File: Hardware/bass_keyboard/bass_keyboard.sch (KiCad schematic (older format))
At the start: 164 parts

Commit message: Added labels to switches
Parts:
- gave numbers to parts that had none: 82

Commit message: Added footprints for diodes
Having trouble finding the footprints for the switches
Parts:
- D1: renamed from D; footprint (none) -> Diode_SMD:D_SOD-123
- D10, D11, D12, D13, D14, D15, D16, D17, D18, D19, D2, D20, D21, D22, D23, D24, D25, D26, D27, D28, D29, D3, D30, D31, D32, D33, D34, D35, D36, D37, D38, D39, D4, D40, D41, D42, D43, D44, D45, D46, D47, D48, D49, D5, D50, D51, D52, D53, D54, D55, D56, D57, D58, D59, D6, D60, D61, D62, D63, D64, D65, D66, D67, D68, D69, D7, D70, D71, D72, D73, D74, D75, D76, D77, D78, D79, D8, D80, D81, D82, D9: renamed from D?; footprint (none) -> Diode_SMD:D_SOD-123
- renumbered MX_Ab-root to MX_Ab-root1, MX_Ab_3rd to MX_Ab_3rd1, MX_Ab_dim to MX_Ab_dim1, MX_Ab_maj to MX_Ab_maj1, MX_Ab_min to MX_Ab_min1, MX_An_3rd to MX_An_3rd1, MX_An_dim to MX_An_dim1, MX_An_maj to MX_An_maj1, MX_An_min to MX_An_min1, MX_An_root to MX_An_root1, MX_Bb_3rd to MX_Bb_3rd1, MX_Bb_dim to MX_Bb_dim1, MX_Bb_maj to MX_Bb_maj1, MX_Bb_min to MX_Bb_min1, MX_Bb_root to MX_Bb_root1, MX_Bn_3rd to MX_Bn_3rd1, MX_Bn_dim to MX_Bn_dim1, MX_Bn_maj to MX_Bn_maj1, MX_Bn_min to MX_Bn_min1, MX_Bn_root to MX_Bn_root1, MX_Cn_3rd to MX_Cn_3rd1, MX_Cn_dim to MX_Cn_dim1, MX_Cn_maj to MX_Cn_maj1, MX_Cn_min to MX_Cn_min1, MX_Cn_root to MX_Cn_root1, MX_Db_3rd to MX_Db_3rd1, MX_Db_dim to MX_Db_dim1, MX_Db_maj to MX_Db_maj1, MX_Db_min to MX_Db_min1, MX_Db_root to MX_Db_root1, MX_Dn_3rd to MX_Dn_3rd1, MX_Dn_dim to MX_Dn_dim1, MX_Dn_maj to MX_Dn_maj1, MX_Dn_min to MX_Dn_min1, MX_Dn_root to MX_Dn_root1, MX_Eb_3rd to MX_Eb_3rd1, MX_Eb_dim to MX_Eb_dim1, MX_Eb_maj to MX_Eb_maj1, MX_Eb_min to MX_Eb_min1, MX_Eb_root to MX_Eb_root1, MX_En_3rd to MX_En_3rd1, MX_En_dim to MX_En_dim1, MX_En_maj to MX_En_maj1, MX_En_min to MX_En_min1, MX_En_root to MX_En_root1, MX_Fn_3rd to MX_Fn_3rd1, MX_Fn_dim to MX_Fn_dim1, MX_Fn_maj to MX_Fn_maj1, MX_Fn_min to MX_Fn_min1, MX_Fn_root to MX_Fn_root1, MX_Fs_3rd to MX_Fs_3rd1, MX_Fs_dim to MX_Fs_dim1, MX_Fs_maj to MX_Fs_maj1, MX_Fs_min to MX_Fs_min1, MX_Fs_root to MX_Fs_root1, MX_Gn_3rd to MX_Gn_3rd1, MX_Gn_dim to MX_Gn_dim1, MX_Gn_maj to MX_Gn_maj1, MX_Gn_min to MX_Gn_min1, MX_Gn_root to MX_Gn_root1, MX_bassbar to MX_bassbar1, MX_dim_aug to MX_dim_aug1, MX_down_half to MX_down_half1, MX_down_oct to MX_down_oct1, MX_keysel_left to MX_keysel_left1, MX_keysel_right to MX_keysel_right1, MX_maj_dom to MX_maj_dom1, MX_trans_reset to MX_trans_reset1, MX_up_half to MX_up_half1, MX_up_oct to MX_up_oct1

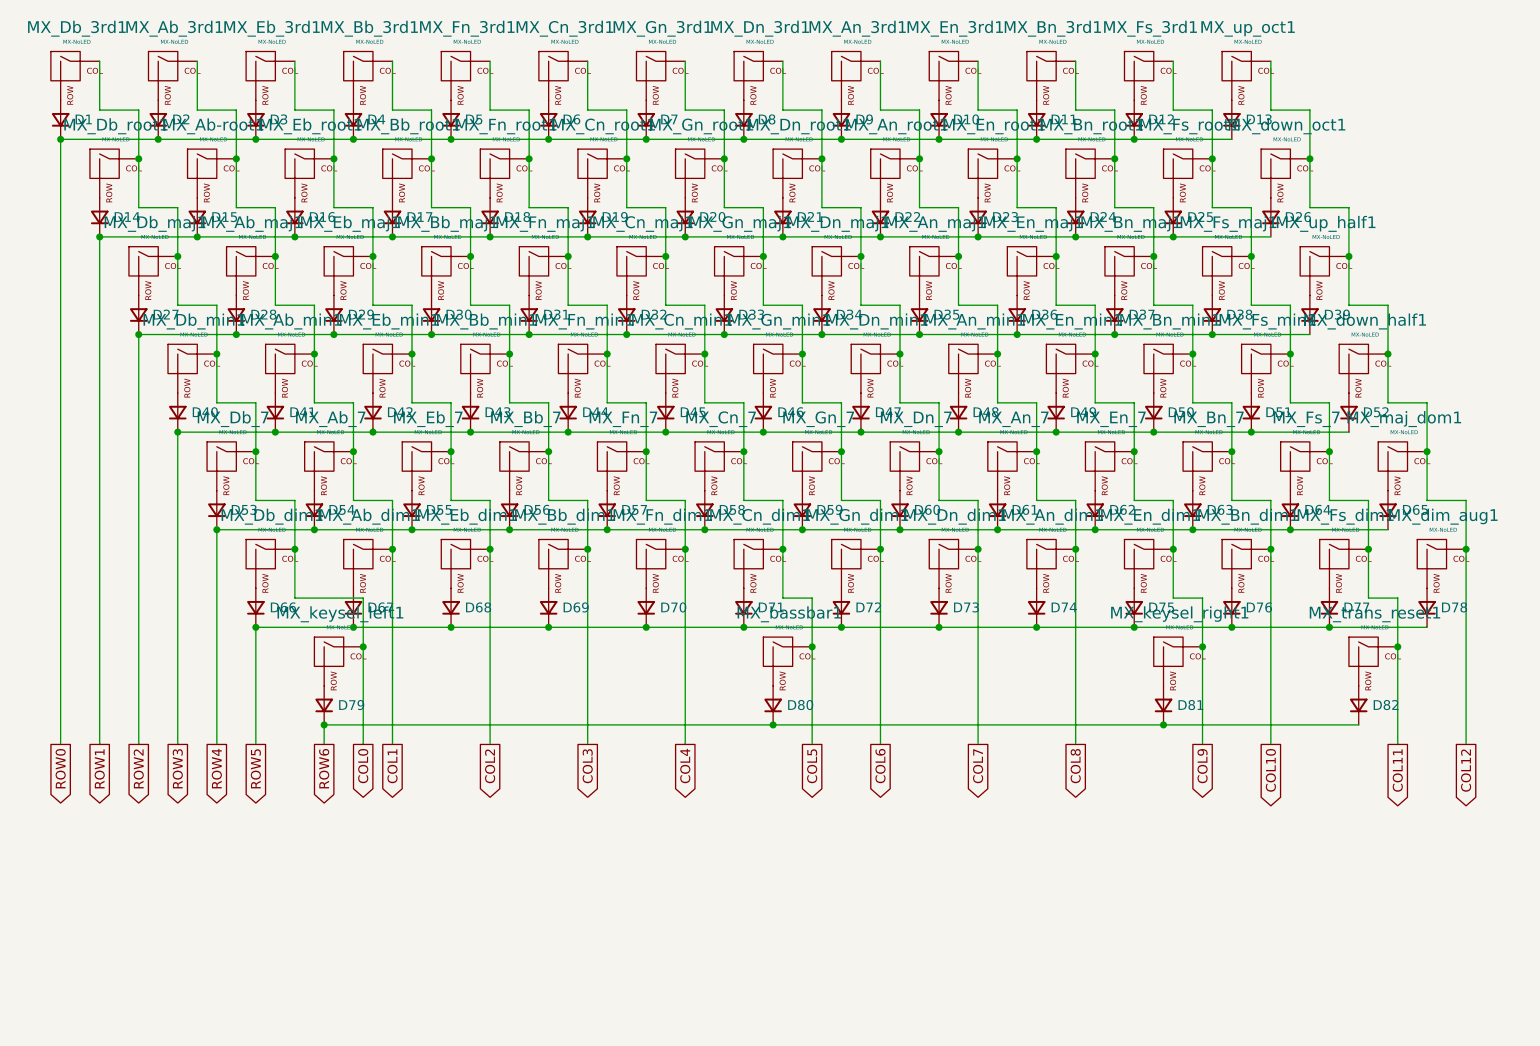
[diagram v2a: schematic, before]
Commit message: Added female connector
Added the connector for the cable to the logic module on the bass keyboard schematic
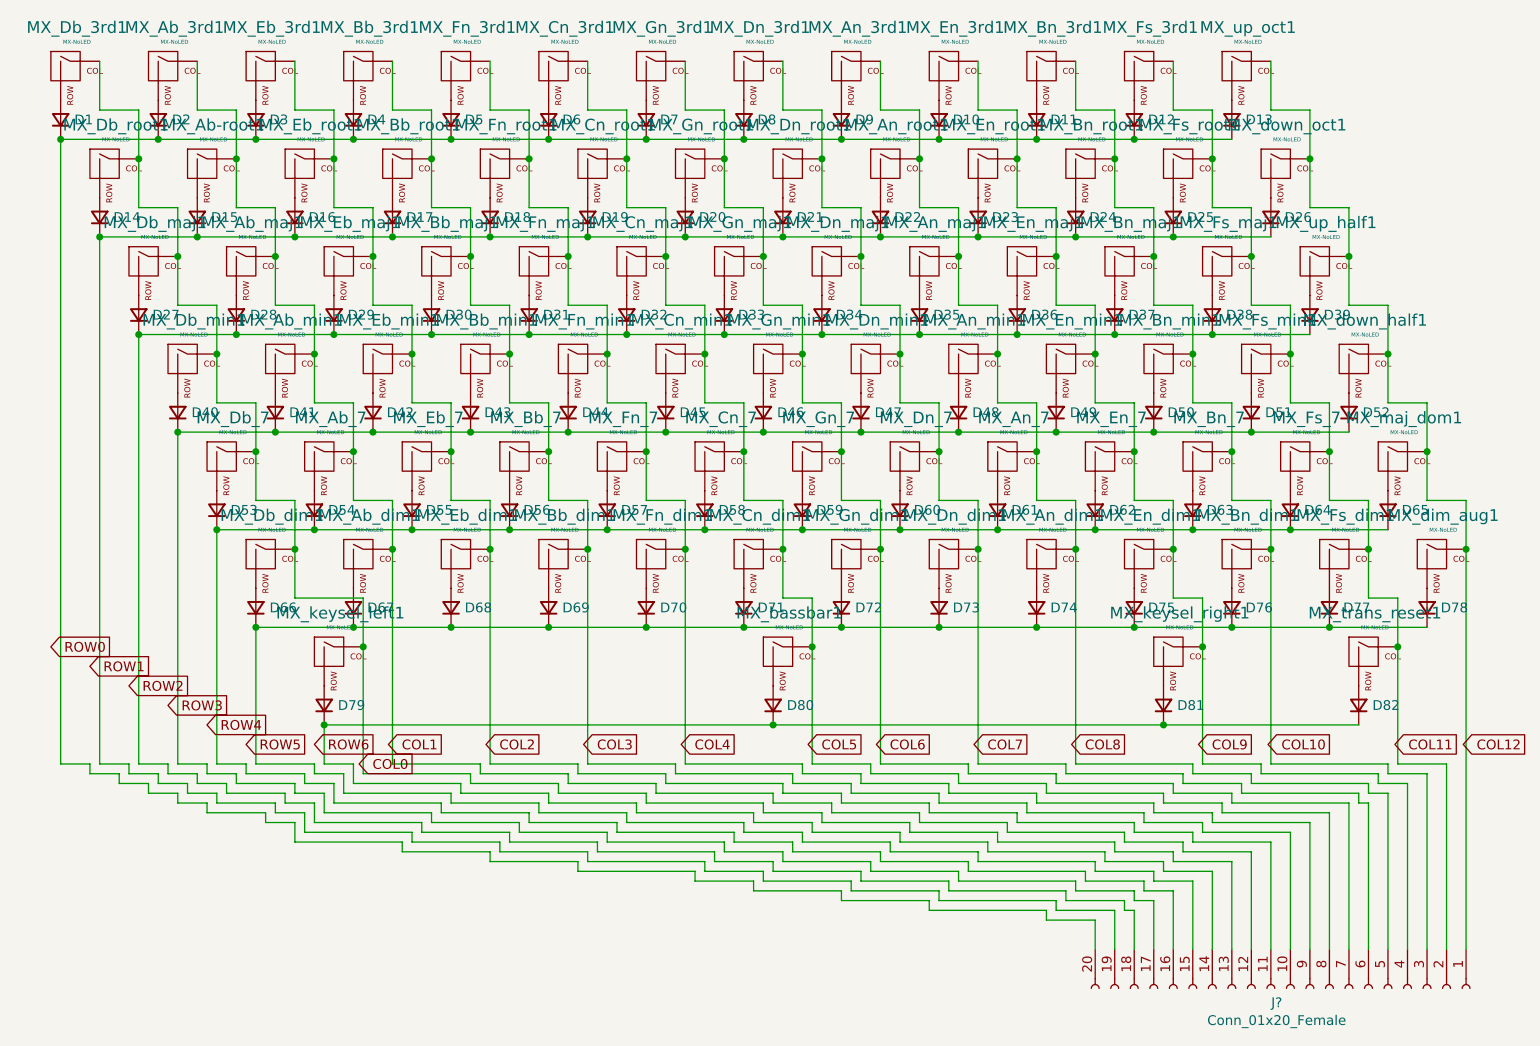
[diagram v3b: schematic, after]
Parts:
- added J?: Conn_01x20_Female, symbol Connector:Conn_01x20_Female
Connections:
- net COL0: now also MX_Ab-root1.1 (COL), MX_Ab_3rd1.1 (COL), MX_Ab_7.1 (COL), MX_Ab_dim1.1 (COL), MX_Ab_maj1.1 (COL), MX_Ab_min1.1 (COL), J?.12 (Pin_12); no longer MX_Db_3rd1.1 (COL), MX_Db_7.1 (COL), MX_Db_dim1.1 (COL), MX_Db_maj1.1 (COL), MX_Db_min1.1 (COL), MX_Db_root1.1 (COL), MX_keysel_left1.1 (COL)
- net COL1: no longer MX_Ab-root1.1 (COL), MX_Ab_3rd1.1 (COL), MX_Ab_7.1 (COL), MX_Ab_dim1.1 (COL), MX_Ab_maj1.1 (COL), MX_Ab_min1.1 (COL)
- net COL10: no longer MX_Bn_3rd1.1 (COL), MX_Bn_7.1 (COL), MX_Bn_dim1.1 (COL), MX_Bn_maj1.1 (COL), MX_Bn_min1.1 (COL), MX_Bn_root1.1 (COL)
- net COL11: no longer MX_Fs_3rd1.1 (COL), MX_Fs_7.1 (COL), MX_Fs_dim1.1 (COL), MX_Fs_maj1.1 (COL), MX_Fs_min1.1 (COL), MX_Fs_root1.1 (COL), MX_trans_reset1.1 (COL)
- net COL12: no longer MX_dim_aug1.1 (COL), MX_down_half1.1 (COL), MX_down_oct1.1 (COL), MX_maj_dom1.1 (COL), MX_up_half1.1 (COL), MX_up_oct1.1 (COL)
- net COL2: no longer MX_Eb_3rd1.1 (COL), MX_Eb_7.1 (COL), MX_Eb_dim1.1 (COL), MX_Eb_maj1.1 (COL), MX_Eb_min1.1 (COL), MX_Eb_root1.1 (COL)
- net COL3: no longer MX_Bb_3rd1.1 (COL), MX_Bb_7.1 (COL), MX_Bb_dim1.1 (COL), MX_Bb_maj1.1 (COL), MX_Bb_min1.1 (COL), MX_Bb_root1.1 (COL)
- net COL4: no longer MX_Fn_3rd1.1 (COL), MX_Fn_7.1 (COL), MX_Fn_dim1.1 (COL), MX_Fn_maj1.1 (COL), MX_Fn_min1.1 (COL), MX_Fn_root1.1 (COL)
- net COL5: no longer MX_Cn_3rd1.1 (COL), MX_Cn_7.1 (COL), MX_Cn_dim1.1 (COL), MX_Cn_maj1.1 (COL), MX_Cn_min1.1 (COL), MX_Cn_root1.1 (COL), MX_bassbar1.1 (COL)
- net COL6: no longer MX_Gn_3rd1.1 (COL), MX_Gn_7.1 (COL), MX_Gn_dim1.1 (COL), MX_Gn_maj1.1 (COL), MX_Gn_min1.1 (COL), MX_Gn_root1.1 (COL)
- net COL7: no longer MX_Dn_3rd1.1 (COL), MX_Dn_7.1 (COL), MX_Dn_dim1.1 (COL), MX_Dn_maj1.1 (COL), MX_Dn_min1.1 (COL), MX_Dn_root1.1 (COL)
- net COL8: no longer MX_An_3rd1.1 (COL), MX_An_7.1 (COL), MX_An_dim1.1 (COL), MX_An_maj1.1 (COL), MX_An_min1.1 (COL), MX_An_root1.1 (COL)
- net COL9: no longer MX_En_3rd1.1 (COL), MX_En_7.1 (COL), MX_En_dim1.1 (COL), MX_En_maj1.1 (COL), MX_En_min1.1 (COL), MX_En_root1.1 (COL), MX_keysel_right1.1 (COL)
- net ROW0: no longer D1.1 (K), D10.1 (K), D11.1 (K), D12.1 (K), D13.1 (K), D2.1 (K), D3.1 (K), D4.1 (K), D5.1 (K), D6.1 (K), D7.1 (K), D8.1 (K), D9.1 (K)
- net ROW1: no longer D14.1 (K), D15.1 (K), D16.1 (K), D17.1 (K), D18.1 (K), D19.1 (K), D20.1 (K), D21.1 (K), D22.1 (K), D23.1 (K), D24.1 (K), D25.1 (K), D26.1 (K)
- net ROW2: no longer D27.1 (K), D28.1 (K), D29.1 (K), D30.1 (K), D31.1 (K), D32.1 (K), D33.1 (K), D34.1 (K), D35.1 (K), D36.1 (K), D37.1 (K), D38.1 (K), D39.1 (K)
- net ROW3: no longer D40.1 (K), D41.1 (K), D42.1 (K), D43.1 (K), D44.1 (K), D45.1 (K), D46.1 (K), D47.1 (K), D48.1 (K), D49.1 (K), D50.1 (K), D51.1 (K), D52.1 (K)
- net ROW4: no longer D53.1 (K), D54.1 (K), D55.1 (K), D56.1 (K), D57.1 (K), D58.1 (K), D59.1 (K), D60.1 (K), D61.1 (K), D62.1 (K), D63.1 (K), D64.1 (K), D65.1 (K)
- net ROW5: no longer D66.1 (K), D67.1 (K), D68.1 (K), D69.1 (K), D70.1 (K), D71.1 (K), D72.1 (K), D73.1 (K), D74.1 (K), D75.1 (K), D76.1 (K), D77.1 (K), D78.1 (K)
- net ROW6: no longer D79.1 (K), D80.1 (K), D81.1 (K), D82.1 (K)
- new net: J?.13 (Pin_13), MX_Db_3rd1.1 (COL), MX_Db_7.1 (COL), MX_Db_dim1.1 (COL), MX_Db_maj1.1 (COL), MX_Db_min1.1 (COL), MX_Db_root1.1 (COL), MX_keysel_left1.1 (COL)
- new net: J?.11 (Pin_11), MX_Eb_3rd1.1 (COL), MX_Eb_7.1 (COL), MX_Eb_dim1.1 (COL), MX_Eb_maj1.1 (COL), MX_Eb_min1.1 (COL), MX_Eb_root1.1 (COL)
- new net: J?.10 (Pin_10), MX_Bb_3rd1.1 (COL), MX_Bb_7.1 (COL), MX_Bb_dim1.1 (COL), MX_Bb_maj1.1 (COL), MX_Bb_min1.1 (COL), MX_Bb_root1.1 (COL)
- new net: J?.9 (Pin_9), MX_Fn_3rd1.1 (COL), MX_Fn_7.1 (COL), MX_Fn_dim1.1 (COL), MX_Fn_maj1.1 (COL), MX_Fn_min1.1 (COL), MX_Fn_root1.1 (COL)
- new net: J?.8 (Pin_8), MX_Cn_3rd1.1 (COL), MX_Cn_7.1 (COL), MX_Cn_dim1.1 (COL), MX_Cn_maj1.1 (COL), MX_Cn_min1.1 (COL), MX_Cn_root1.1 (COL), MX_bassbar1.1 (COL)
- new net: J?.7 (Pin_7), MX_Gn_3rd1.1 (COL), MX_Gn_7.1 (COL), MX_Gn_dim1.1 (COL), MX_Gn_maj1.1 (COL), MX_Gn_min1.1 (COL), MX_Gn_root1.1 (COL)
- new net: J?.6 (Pin_6), MX_Dn_3rd1.1 (COL), MX_Dn_7.1 (COL), MX_Dn_dim1.1 (COL), MX_Dn_maj1.1 (COL), MX_Dn_min1.1 (COL), MX_Dn_root1.1 (COL)
- new net: J?.5 (Pin_5), MX_An_3rd1.1 (COL), MX_An_7.1 (COL), MX_An_dim1.1 (COL), MX_An_maj1.1 (COL), MX_An_min1.1 (COL), MX_An_root1.1 (COL)
- new net: J?.4 (Pin_4), MX_En_3rd1.1 (COL), MX_En_7.1 (COL), MX_En_dim1.1 (COL), MX_En_maj1.1 (COL), MX_En_min1.1 (COL), MX_En_root1.1 (COL), MX_keysel_right1.1 (COL)
- new net: J?.3 (Pin_3), MX_Bn_3rd1.1 (COL), MX_Bn_7.1 (COL), MX_Bn_dim1.1 (COL), MX_Bn_maj1.1 (COL), MX_Bn_min1.1 (COL), MX_Bn_root1.1 (COL)
- new net: J?.2 (Pin_2), MX_Fs_3rd1.1 (COL), MX_Fs_7.1 (COL), MX_Fs_dim1.1 (COL), MX_Fs_maj1.1 (COL), MX_Fs_min1.1 (COL), MX_Fs_root1.1 (COL), MX_trans_reset1.1 (COL)
- new net: J?.1 (Pin_1), MX_dim_aug1.1 (COL), MX_down_half1.1 (COL), MX_down_oct1.1 (COL), MX_maj_dom1.1 (COL), MX_up_half1.1 (COL), MX_up_oct1.1 (COL)
- new net: D1.1 (K), D10.1 (K), D11.1 (K), D12.1 (K), D13.1 (K), D2.1 (K), D3.1 (K), D4.1 (K), D5.1 (K), D6.1 (K), D7.1 (K), D8.1 (K), D9.1 (K), J?.20 (Pin_20)
- new net: D14.1 (K), D15.1 (K), D16.1 (K), D17.1 (K), D18.1 (K), D19.1 (K), D20.1 (K), D21.1 (K), D22.1 (K), D23.1 (K), D24.1 (K), D25.1 (K), D26.1 (K), J?.19 (Pin_19)
- new net: D79.1 (K), D80.1 (K), D81.1 (K), D82.1 (K), J?.14 (Pin_14)
- new net: D66.1 (K), D67.1 (K), D68.1 (K), D69.1 (K), D70.1 (K), D71.1 (K), D72.1 (K), D73.1 (K), D74.1 (K), D75.1 (K), D76.1 (K), D77.1 (K), D78.1 (K), J?.15 (Pin_15)
- new net: D53.1 (K), D54.1 (K), D55.1 (K), D56.1 (K), D57.1 (K), D58.1 (K), D59.1 (K), D60.1 (K), D61.1 (K), D62.1 (K), D63.1 (K), D64.1 (K), D65.1 (K), J?.16 (Pin_16)
- new net: D40.1 (K), D41.1 (K), D42.1 (K), D43.1 (K), D44.1 (K), D45.1 (K), D46.1 (K), D47.1 (K), D48.1 (K), D49.1 (K), D50.1 (K), D51.1 (K), D52.1 (K), J?.17 (Pin_17)
- new net: D27.1 (K), D28.1 (K), D29.1 (K), D30.1 (K), D31.1 (K), D32.1 (K), D33.1 (K), D34.1 (K), D35.1 (K), D36.1 (K), D37.1 (K), D38.1 (K), D39.1 (K), J?.18 (Pin_18)
